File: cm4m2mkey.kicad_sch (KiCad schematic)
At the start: 26 parts, among them J8 1-2199119-6

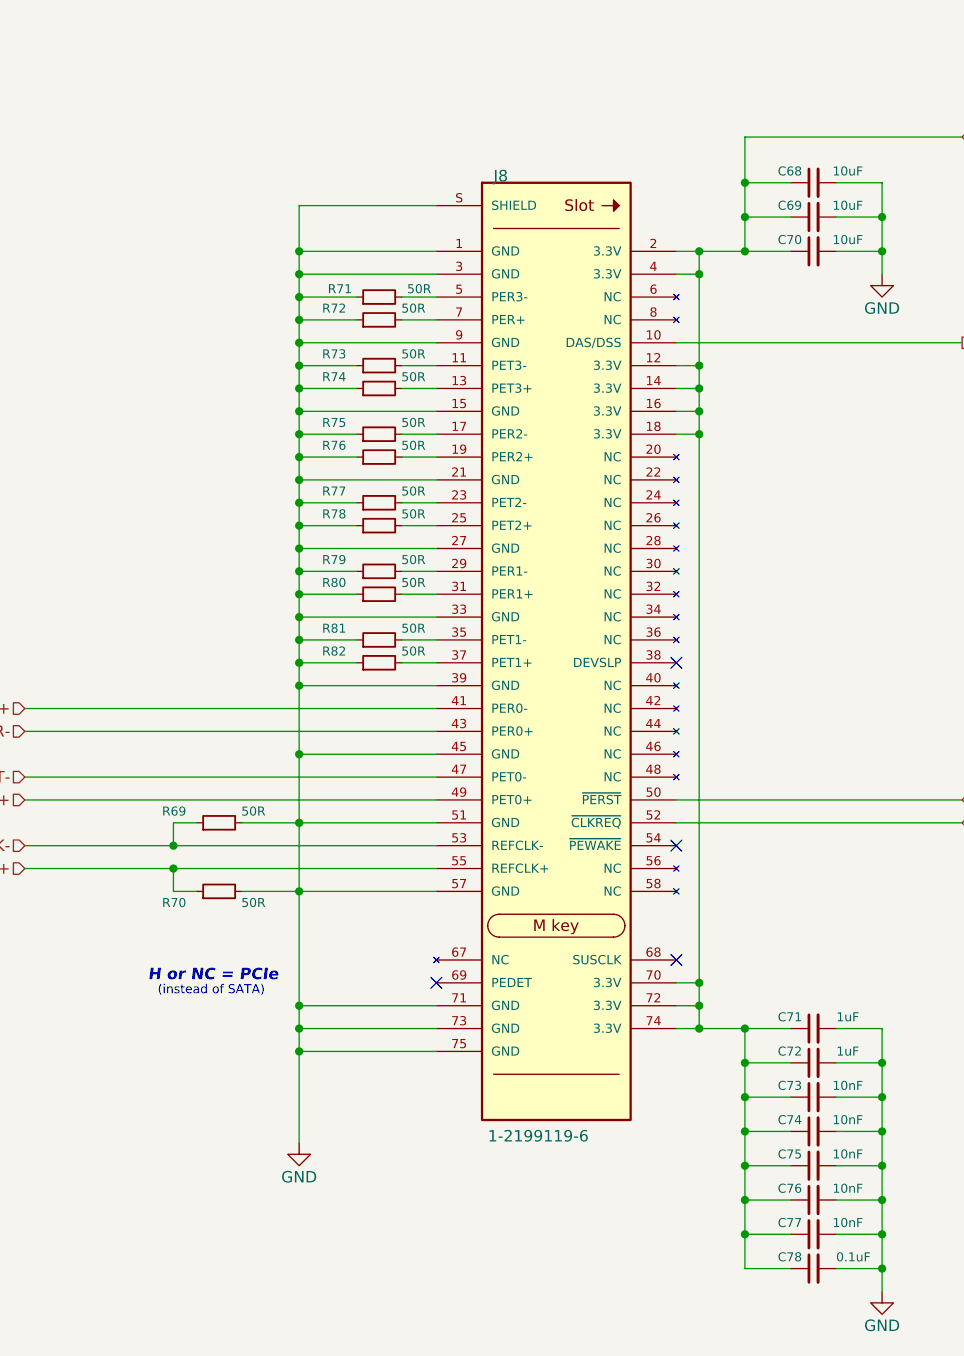
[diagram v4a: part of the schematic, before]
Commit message: connecterized faceplate, refreshed schematic
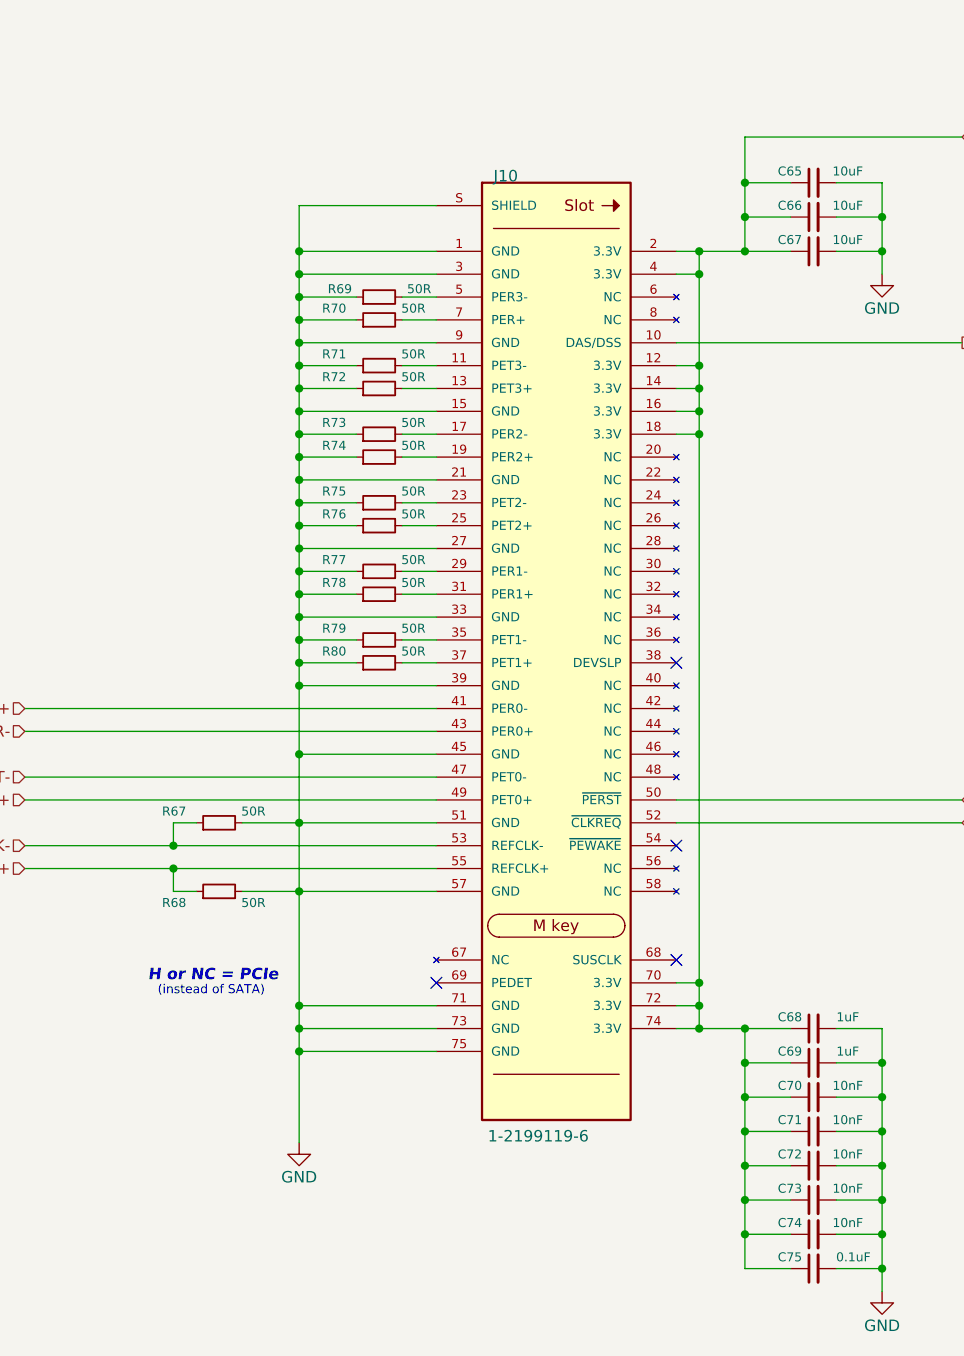
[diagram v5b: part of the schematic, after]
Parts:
- renumbered C68 to C65, C69 to C66, C70 to C67, C71 to C68, C72 to C69, C73 to C70, C74 to C71, C75 to C72, C76 to C73, C77 to C74, C78 to C75, J8 to J10, R69 to R67, R70 to R68, R71 to R69, R72 to R70, R73 to R71, R74 to R72, R75 to R73, R76 to R74, R77 to R75, R78 to R76, R79 to R77, R80 to R78, R81 to R79, R82 to R80
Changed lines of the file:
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@@
   (symbol (lib_id "Device:R_Small") (at 81.28 118.11 90) (unit 1)
     (in_bom yes) (on_board yes)
-    (property "Reference" "R69" (id 0) (at 74.93 116.84 90)
+    (property "Reference" "R67" (id 0) (at 74.93 116.84 90)
       (effects (font (size 1 1)) (justify right))
     )
@@
   (symbol (lib_id "Device:R_Small") (at 99.06 77.47 90) (unit 1)
     (in_bom yes) (on_board yes)
-    (property "Reference" "R76" (id 0) (at 92.71 76.2 90)
+    (property "Reference" "R74" (id 0) (at 92.71 76.2 90)
       (effects (font (size 1 1)) (justify right))
     )
@@
   (symbol (lib_id "Device:C_Small") (at 147.32 54.61 90) (unit 1)
     (in_bom yes) (on_board yes)
-    (property "Reference" "C70" (id 0) (at 146.05 53.34 90)
+    (property "Reference" "C67" (id 0) (at 146.05 53.34 90)
       (effects (font (size 1 1)) (justify left))
     )
@@
   (symbol (lib_id "Device:R_Small") (at 99.06 82.55 90) (unit 1)
     (in_bom yes) (on_board yes)
-    (property "Reference" "R77" (id 0) (at 92.71 81.28 90)
+    (property "Reference" "R75" (id 0) (at 92.71 81.28 90)
       (effects (font (size 1 1)) (justify right))
     )
@@
   (symbol (lib_id "Device:C_Small") (at 147.32 167.64 90) (unit 1)
     (in_bom yes) (on_board yes)
-    (property "Reference" "C78" (id 0) (at 146.05 166.37 90)
+    (property "Reference" "C75" (id 0) (at 146.05 166.37 90)
       (effects (font (size 1 1)) (justify left))
     )
@@
   (symbol (lib_id "Device:R_Small") (at 99.06 74.93 90) (unit 1)
     (in_bom yes) (on_board yes)
-    (property "Reference" "R75" (id 0) (at 92.71 73.66 90)
+    (property "Reference" "R73" (id 0) (at 92.71 73.66 90)
       (effects (font (size 1 1)) (justify right))
     )
@@
   (symbol (lib_id "Device:R_Small") (at 99.06 59.69 90) (unit 1)
     (in_bom yes) (on_board yes)
-    (property "Reference" "R71" (id 0) (at 93.345 58.801 90)
+    (property "Reference" "R69" (id 0) (at 93.345 58.801 90)
       (effects (font (size 1 1)) (justify right))
     )
@@
   (symbol (lib_id "Device:R_Small") (at 99.06 67.31 90) (unit 1)
     (in_bom yes) (on_board yes)
-    (property "Reference" "R73" (id 0) (at 92.71 66.04 90)
+    (property "Reference" "R71" (id 0) (at 92.71 66.04 90)
       (effects (font (size 1 1)) (justify right))
     )
@@
   (symbol (lib_id "Device:C_Small") (at 147.32 152.4 90) (unit 1)
     (in_bom yes) (on_board yes)
-    (property "Reference" "C74" (id 0) (at 146.05 151.13 90)
+    (property "Reference" "C71" (id 0) (at 146.05 151.13 90)
       (effects (font (size 1 1)) (justify left))
     )
@@
   (symbol (lib_id "Device:C_Small") (at 147.32 144.78 90) (unit 1)
     (in_bom yes) (on_board yes)
-    (property "Reference" "C72" (id 0) (at 146.05 143.51 90)
+    (property "Reference" "C69" (id 0) (at 146.05 143.51 90)
       (effects (font (size 1 1)) (justify left))
     )
@@
   (symbol (lib_id "Device:C_Small") (at 147.32 140.97 90) (unit 1)
     (in_bom yes) (on_board yes)
-    (property "Reference" "C71" (id 0) (at 146.05 139.7 90)
+    (property "Reference" "C68" (id 0) (at 146.05 139.7 90)
       (effects (font (size 1 1)) (justify left))
     )
@@
   (symbol (lib_id "Device:R_Small") (at 99.06 97.79 90) (unit 1)
     (in_bom yes) (on_board yes)
-    (property "Reference" "R81" (id 0) (at 92.71 96.52 90)
+    (property "Reference" "R79" (id 0) (at 92.71 96.52 90)
       (effects (font (size 1 1)) (justify right))
     )
@@
   (symbol (lib_id "Device:C_Small") (at 147.32 148.59 90) (unit 1)
     (in_bom yes) (on_board yes)
-    (property "Reference" "C73" (id 0) (at 146.05 147.32 90)
+    (property "Reference" "C70" (id 0) (at 146.05 147.32 90)
       (effects (font (size 1 1)) (justify left))
     )
@@
   (symbol (lib_id "Device:C_Small") (at 147.32 46.99 90) (unit 1)
     (in_bom yes) (on_board yes)
-    (property "Reference" "C68" (id 0) (at 146.05 45.72 90)
+    (property "Reference" "C65" (id 0) (at 146.05 45.72 90)
       (effects (font (size 1 1)) (justify left))
     )
@@
   (symbol (lib_id "power:GND") (at 90.17 153.67 0) (unit 1)
     (in_bom yes) (on_board yes)
-    (property "Reference" "#PWR056" (id 0) (at 90.17 160.02 0)
+    (property "Reference" "#PWR055" (id 0) (at 90.17 160.02 0)
       (effects (font (size 1.27 1.27)) hide)
     )
@@
   (symbol (lib_id "power:GND") (at 154.94 170.18 0) (unit 1)
     (in_bom yes) (on_board yes)
-    (property "Reference" "#PWR058" (id 0) (at 154.94 176.53 0)
+    (property "Reference" "#PWR057" (id 0) (at 154.94 176.53 0)
       (effects (font (size 1.27 1.27)) hide)
     )
@@
   (symbol (lib_id "Device:R_Small") (at 99.06 69.85 90) (unit 1)
     (in_bom yes) (on_board yes)
-    (property "Reference" "R74" (id 0) (at 92.71 68.58 90)
+    (property "Reference" "R72" (id 0) (at 92.71 68.58 90)
       (effects (font (size 1 1)) (justify right))
     )
@@
   (symbol (lib_id "Device:C_Small") (at 147.32 163.83 90) (unit 1)
     (in_bom yes) (on_board yes)
-    (property "Reference" "C77" (id 0) (at 146.05 162.56 90)
+    (property "Reference" "C74" (id 0) (at 146.05 162.56 90)
       (effects (font (size 1 1)) (justify left))
     )
@@
   (symbol (lib_id "Device:C_Small") (at 147.32 156.21 90) (unit 1)
     (in_bom yes) (on_board yes)
-    (property "Reference" "C75" (id 0) (at 146.05 154.94 90)
+    (property "Reference" "C72" (id 0) (at 146.05 154.94 90)
       (effects (font (size 1 1)) (justify left))
     )
@@
   (symbol (lib_id "Connector_M.2_TE:1-2199119-6") (at 119.38 99.06 0) (unit 1)
     (in_bom yes) (on_board yes)
-    (property "Reference" "J8" (id 0) (at 111.76 46.99 0)
+    (property "Reference" "J10" (id 0) (at 111.76 46.99 0)
       (effects (font (size 1.27 1.27)) (justify left bottom))
     )
@@
   (symbol (lib_id "power:GND") (at 154.94 57.15 0) (unit 1)
     (in_bom yes) (on_board yes)
-    (property "Reference" "#PWR057" (id 0) (at 154.94 63.5 0)
+    (property "Reference" "#PWR056" (id 0) (at 154.94 63.5 0)
       (effects (font (size 1.27 1.27)) hide)
     )
@@
   (symbol (lib_id "Device:R_Small") (at 99.06 90.17 90) (unit 1)
     (in_bom yes) (on_board yes)
-    (property "Reference" "R79" (id 0) (at 92.71 88.9 90)
+    (property "Reference" "R77" (id 0) (at 92.71 88.9 90)
       (effects (font (size 1 1)) (justify right))
     )
@@
   (symbol (lib_id "Device:R_Small") (at 99.06 62.23 90) (unit 1)
     (in_bom yes) (on_board yes)
-    (property "Reference" "R72" (id 0) (at 92.71 60.96 90)
+    (property "Reference" "R70" (id 0) (at 92.71 60.96 90)
       (effects (font (size 1 1)) (justify right))
     )
@@
   (symbol (lib_id "Device:C_Small") (at 147.32 50.8 90) (unit 1)
     (in_bom yes) (on_board yes)
-    (property "Reference" "C69" (id 0) (at 146.05 49.53 90)
+    (property "Reference" "C66" (id 0) (at 146.05 49.53 90)
       (effects (font (size 1 1)) (justify left))
     )
@@
   (symbol (lib_id "Device:R_Small") (at 81.28 125.73 90) (unit 1)
     (in_bom yes) (on_board yes)
-    (property "Reference" "R70" (id 0) (at 74.93 127 90)
+    (property "Reference" "R68" (id 0) (at 74.93 127 90)
       (effects (font (size 1 1)) (justify right))
     )
@@
   (symbol (lib_id "Device:R_Small") (at 99.06 100.33 90) (unit 1)
     (in_bom yes) (on_board yes)
-    (property "Reference" "R82" (id 0) (at 92.71 99.06 90)
+    (property "Reference" "R80" (id 0) (at 92.71 99.06 90)
       (effects (font (size 1 1)) (justify right))
     )
@@
   (symbol (lib_id "Device:C_Small") (at 147.32 160.02 90) (unit 1)
     (in_bom yes) (on_board yes)
-    (property "Reference" "C76" (id 0) (at 146.05 158.75 90)
+    (property "Reference" "C73" (id 0) (at 146.05 158.75 90)
       (effects (font (size 1 1)) (justify left))
     )
@@
   (symbol (lib_id "Device:R_Small") (at 99.06 85.09 90) (unit 1)
     (in_bom yes) (on_board yes)
-    (property "Reference" "R78" (id 0) (at 92.71 83.82 90)
+    (property "Reference" "R76" (id 0) (at 92.71 83.82 90)
       (effects (font (size 1 1)) (justify right))
     )
@@
   (symbol (lib_id "Device:R_Small") (at 99.06 92.71 90) (unit 1)
     (in_bom yes) (on_board yes)
-    (property "Reference" "R80" (id 0) (at 92.71 91.44 90)
-      (effects (font (size 1 1)) (justify right))
-    )
+    (property "Reference" "R78" (id 0) (at 92.71 91.44 90)
+      (effects (font (size 1 1)) (justify right))
+    )
